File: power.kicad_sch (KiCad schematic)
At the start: 61 parts, among them J1 PWR + CAN harness, Q1 100V 6.8mOhm N-ch, U1 LM74700-Q1, U2 LM5164 (5V), U3 LM5164 (3V3)

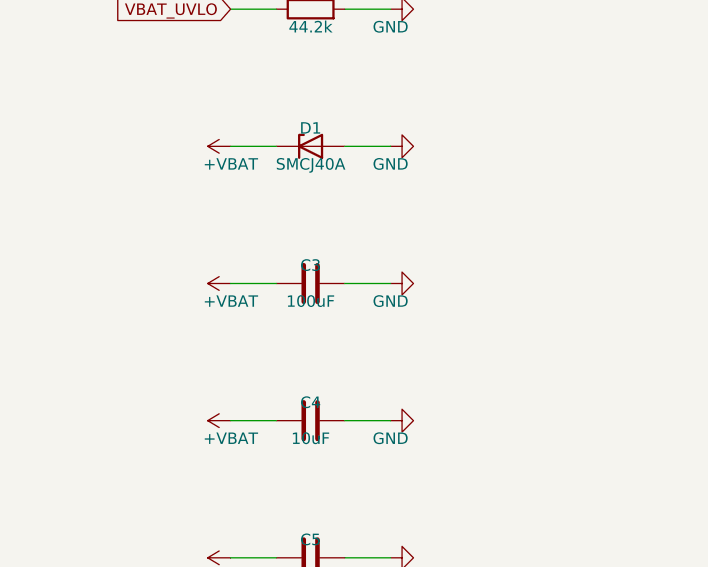
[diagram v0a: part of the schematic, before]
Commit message: Audit every polarised part's orientation; give the electrolytic a polarised symbol
Checked all 17 polarised or orientation-sensitive parts against KiCad's
pin conventions (D_Zener and D_Schottky are 1=K 2=A, LED is 1=K 2=A,
D_TVS is symmetric, D_Schottky_Dual_Series_AKC is 1=A 2=K 3=common) and
against what each one has to do in circuit:

  D1  SMCJ40A     K to +VBAT, A to GND         clamps the positive rail
  D2  MM3Z3V6T1G  K to +3V3                    zener clamps the rail
  D3  SMAJ6.0A    K to +5VS                    clamps the sensor rail
  D4  green LED   A to +3V3, K through R to 0  lights the right way
  D5  PMEG4010    A to VBUS, K to +5V          USB feeds the rail, no back-feed
  D6-D14 (CA)     bidirectional, symbol matches the CA suffix
  BAT54S x5       GND-anode / signal-common / +3V3-cathode, so the pair
                  clamps a fault either side of the rails

All correct. The module is correct too: pin 1 (GND) at the top-left,
rotation 0, pads spanning y 1.54..19.30, and the antenna end -- the end
with no pads -- overhanging the top edge, which is the whole reason it
sits where it does.

The common-mode choke is worth recording because its footprint has
renumbered pads: on the board, pads 1 and 3 are both transceiver-side and
2 and 4 both connector-side, so the two windings run the same way. That
is the dot convention a CMC needs; reverse one winding and it stops
rejecting common mode.

One real finding, now fixed. The bulk electrolytic carried a plain
Device:C on a CP_Elec land. Pin 1 is + on that footprint and pin 1 was
already +VBAT, so the board was right -- but by luck rather than by
construction, with nothing in the schematic showing polarity and no way
for ERC or a reader to catch a reversal. It is Device:C_Polarized now.

Co-Authored-By: Claude Opus 5 <noreply@anthropic.com>
Claude-Session: https://claude.ai/code/session_01DhNbL25h25p8VFCjRfJik9
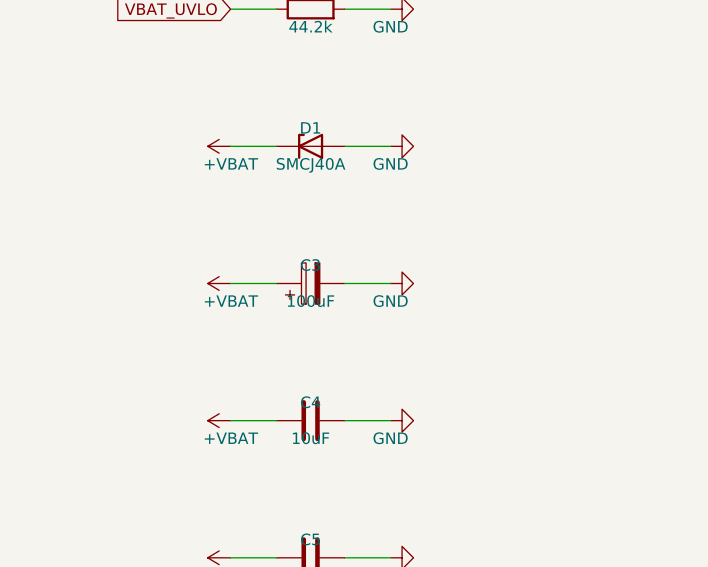
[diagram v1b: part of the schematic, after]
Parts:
- C3: symbol Device:C -> Device:C_Polarized; Note Bulk hold-up; any 100uF >=80V SMD electrolytic on a 10x10.5 land works -- match in the JLC catalog at order -> Bulk hold-up; any 100uF >=80V SMD electrolytic on a 10x10.5 land works -- match in the JLC catalog at order. Pin 1 is +
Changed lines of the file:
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@@
     )
   )
-  (symbol (lib_id "Device:C") (at 44.45 226.06 90) (unit 1)
+  (symbol (lib_id "Device:C_Polarized") (at 44.45 226.06 90) (unit 1)
     (in_bom yes) (on_board yes) (dnp no)
     (property "Reference" "C3" (at 44.45 224.06 270)
@@
       (effects (font (size 1.27 1.27)) hide)
     )
-    (property "Note" "Bulk hold-up; any 100uF >=80V SMD electrolytic on a 10x10.5 land works -- match in the JLC catalog at order" (at 44.45 228.06 270)
+    (property "Note" "Bulk hold-up; any 100uF >=80V SMD electrolytic on a 10x10.5 land works -- match in the JLC catalog at order. Pin 1 is +" (at 44.45 228.06 270)
       (effects (font (size 1.27 1.27)) hide)
     )

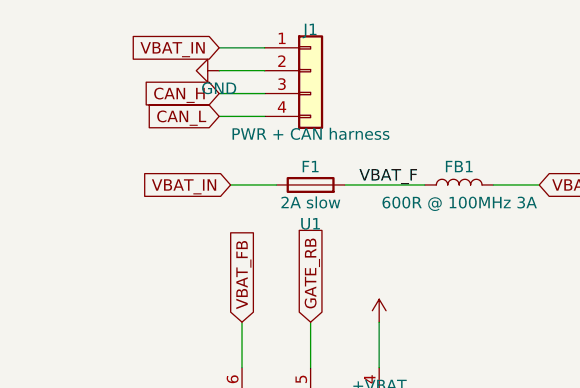
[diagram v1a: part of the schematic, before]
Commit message: Schematic: make the hierarchy real; trunk layout does not decompose
The six sheets were pages, not a hierarchy: every cross-sheet connection
went by global label and no sheet declared an interface. Now the 40 nets
that actually leave a sheet carry hierarchical labels there and appear as
pins on that sheet's symbol at the root, so each block states what it
needs and what it provides. Rails stay global, since a power symbol is
global by definition and does not belong in a signal interface.

Three things had to be right for KiCad to see it, and each announced
itself: dropping both pin labels on a wired net let KiCad autoname it and
validate.py caught the rename; a label anchored 0.6 mm off its wire is a
floating label and ERC said so; and 40 and 32 are not multiples of the
1.27 mm connection grid, so every pin and stub landed off-grid until the
sheets moved to 40.64. The last one hid a real bug -- the sheet symbol
stayed at x=40 while its pins moved to 40.64, leaving them 0.64 mm off
the sheet edge and every one of them unconnected.

On the trunk layout: I measured it rather than attempting it blind, and
it does not decompose into a bounded job. Of ~98 nets, 21 have the
two-pin shape already wired, 40 cross sheets and now have hierarchical
labels, and 37 are multi-pin local nodes -- the ones a person draws as a
wire tree. A trunk needs every part on the node placed against it, but
each two-pin part sits between two different nets, so trunking one net
fixes the position its other net then has to work around. That is
schematic auto-layout, not a special case of it. Restricting to nodes
whose members all end on a rail, which is the one tractable subset, finds
6 of the 37. Six nodes is not worth the machinery, and a half-working
trunk pass would read worse than the honest grid.

Board is untouched by any of this: still 0 DRC errors, 0 unconnected.

Co-Authored-By: Claude Opus 5 <noreply@anthropic.com>
Claude-Session: https://claude.ai/code/session_01DhNbL25h25p8VFCjRfJik9
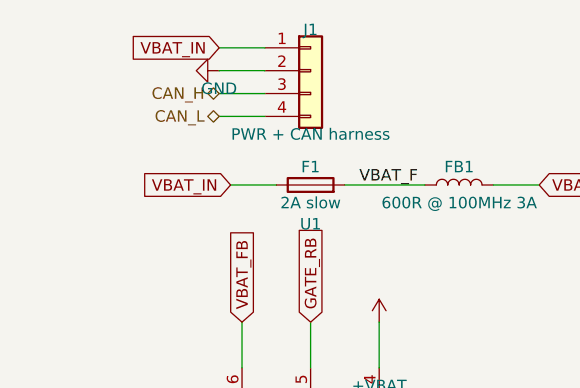
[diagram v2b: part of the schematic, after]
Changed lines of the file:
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@@
     )
   )
-  (global_label "CAN_H" (shape input) (at 34.29 22.86 180) (fields_autoplaced)
+  (hierarchical_label "CAN_H" (shape bidirectional) (at 34.29 22.86 180)
     (effects (font (size 1.27 1.27)) (justify right))
-    (property "Intersheet References" "${INTERSHEET_REFS}" (at 34.29 22.86 0)
-      (effects (font (size 1.27 1.27)) (justify left) hide)
-    )
   )
-  (global_label "CAN_L" (shape input) (at 34.29 25.4 180) (fields_autoplaced)
+  (hierarchical_label "CAN_L" (shape bidirectional) (at 34.29 25.4 180)
     (effects (font (size 1.27 1.27)) (justify right))
-    (property "Intersheet References" "${INTERSHEET_REFS}" (at 34.29 25.4 0)
-      (effects (font (size 1.27 1.27)) (justify left) hide)
-    )
   )
   (global_label "VBAT_IN" (shape input) (at 35.56 33.02 180) (fields_autoplaced)
